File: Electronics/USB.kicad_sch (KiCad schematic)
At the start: 13 parts, among them IC4 USB2512B-AEZG, J24 USB_A_Stacked

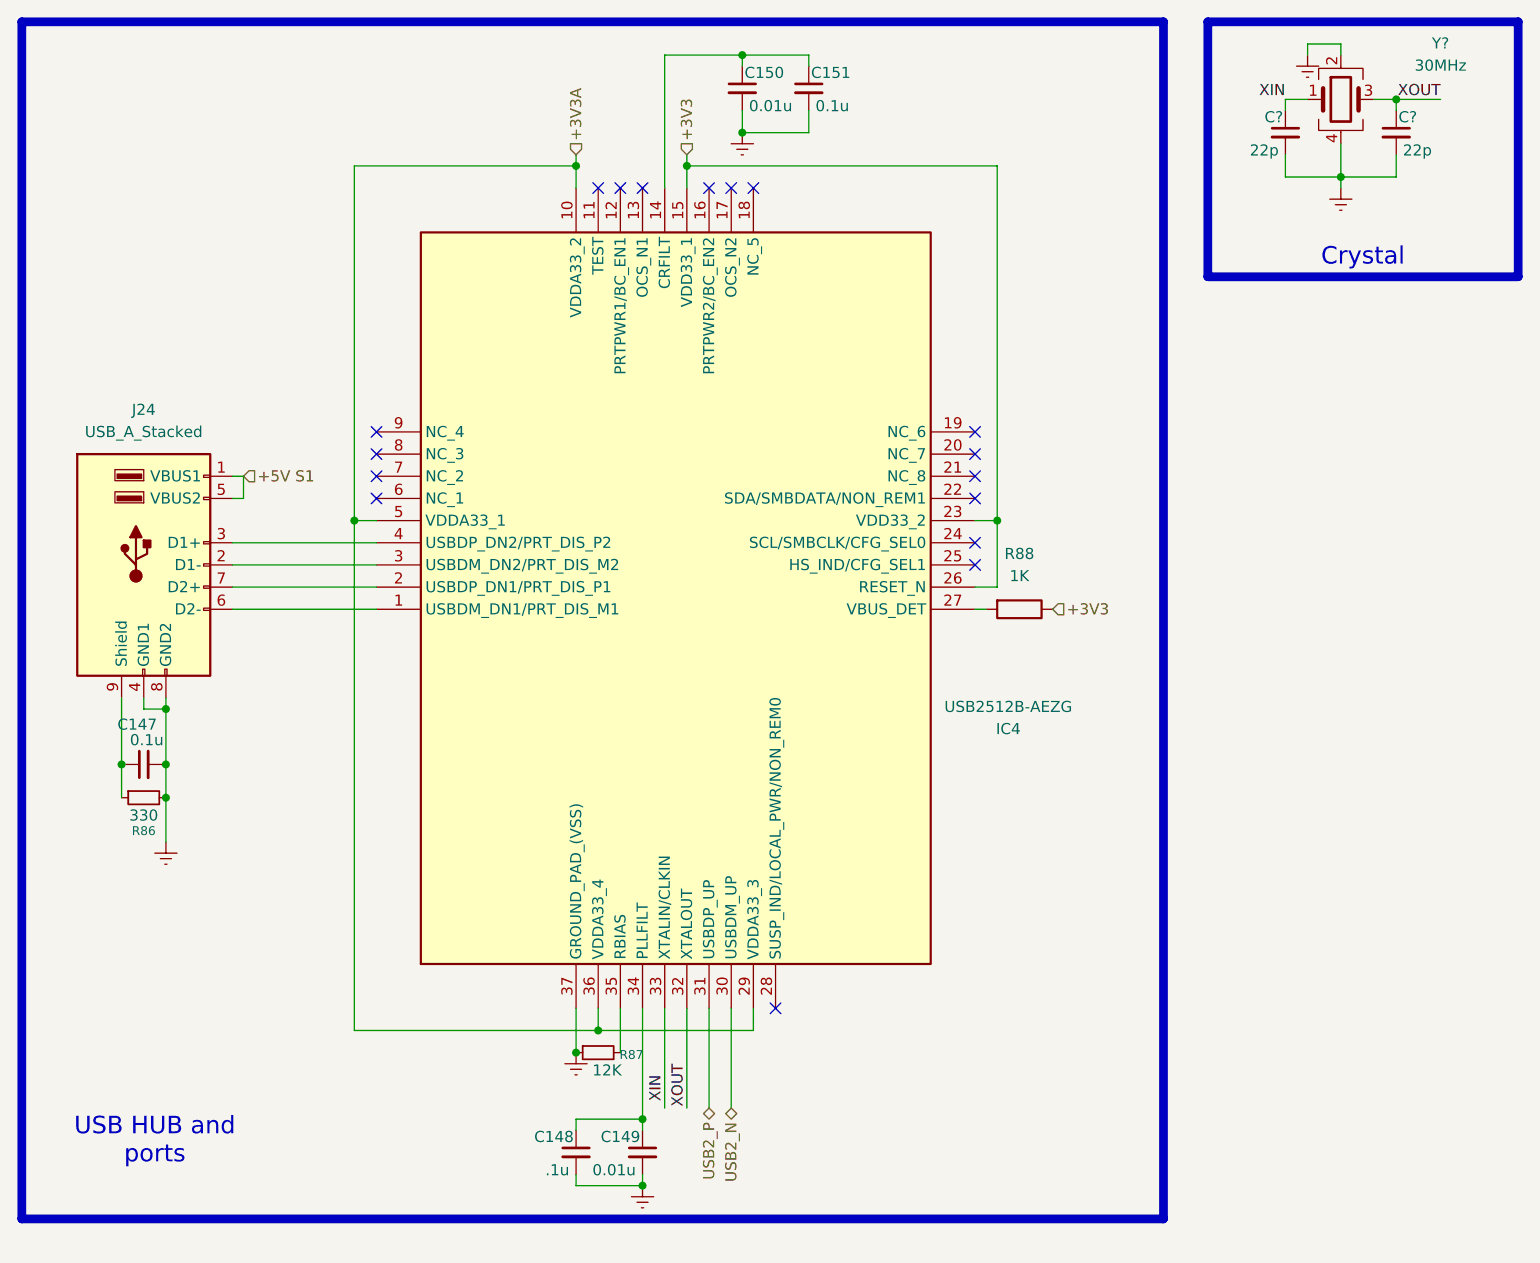
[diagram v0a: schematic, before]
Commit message: Power symbols changed and sata hub fixed schem
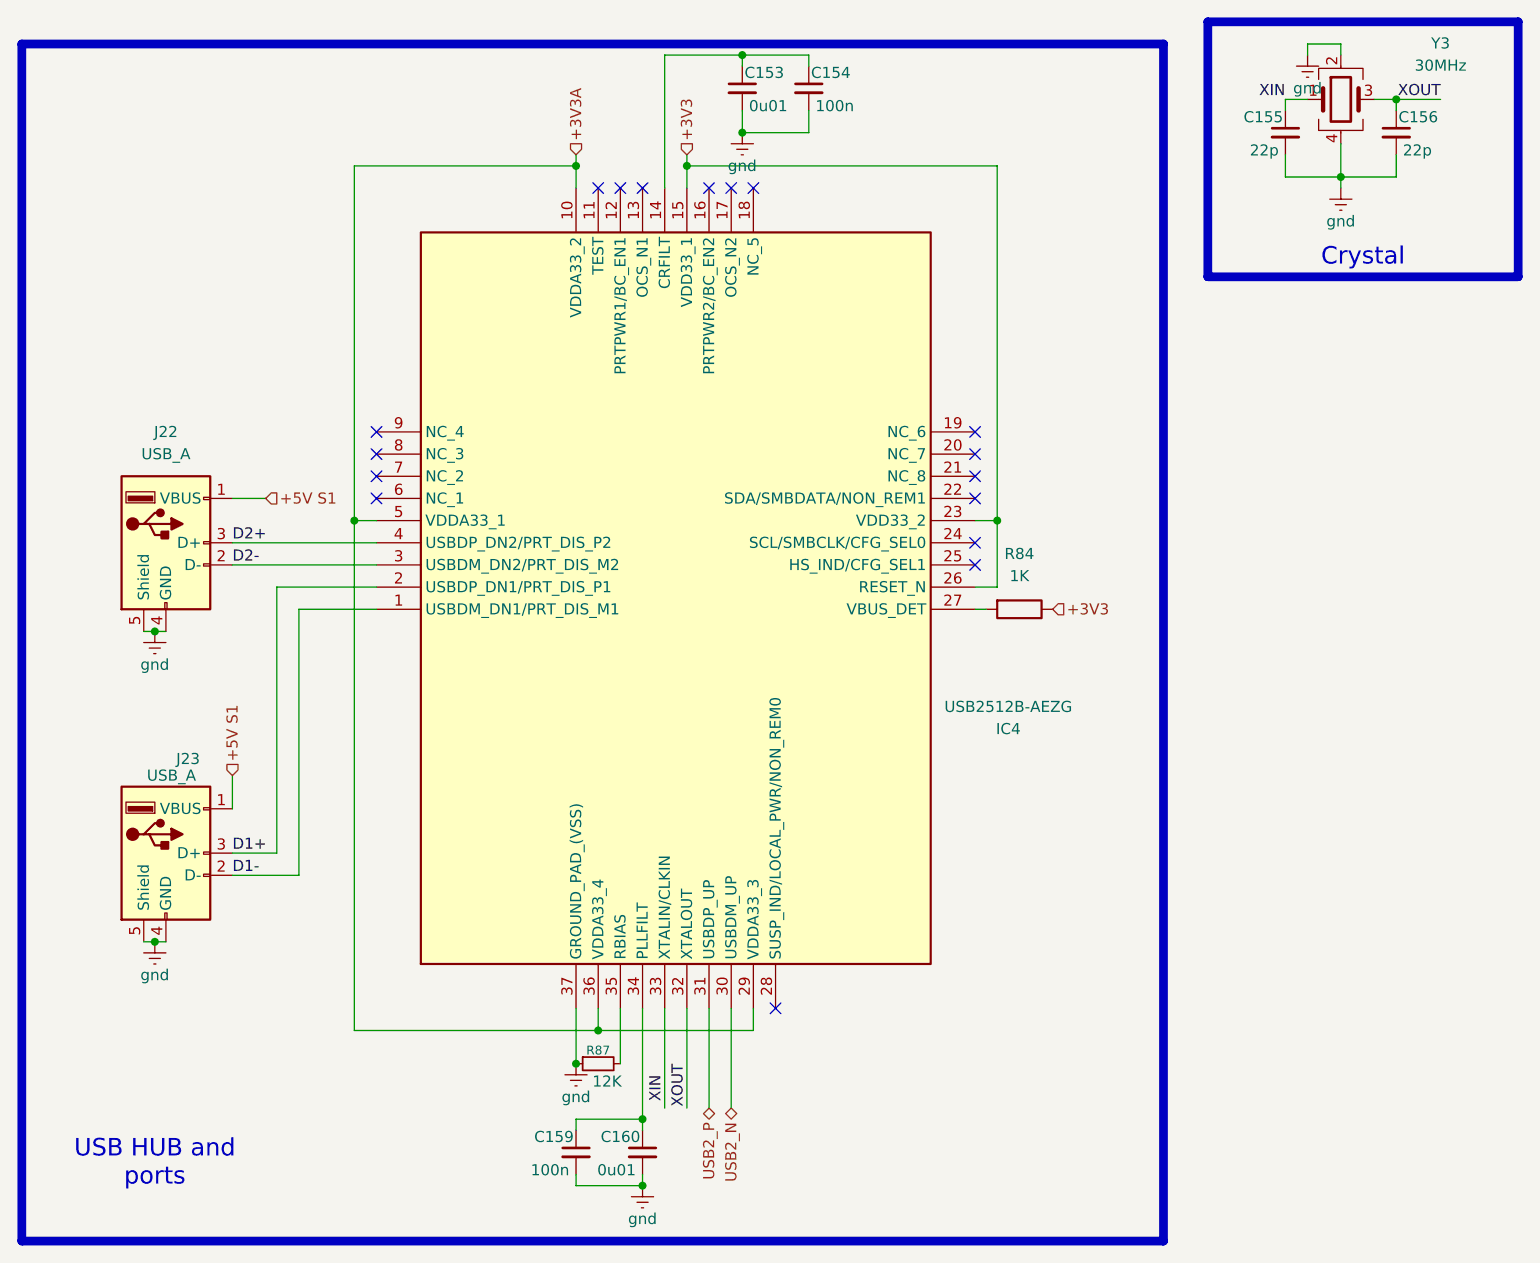
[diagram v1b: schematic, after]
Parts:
- removed C147: 0.1u, Capacitor_SMD:C_0603_1608Metric, symbol Device:C_Small
- removed J24: USB_A_Stacked, Connector_USB:USB_A_Wuerth_61400826021_Horizontal_Stacked, symbol Connector:USB_A_Stacked
- removed R86: 330, Resistor_SMD:R_0603_1608Metric, symbol Device:R_Small
- added J22, J23: USB_A, 482040001:CONN_48204-0001_MOL, symbol Connector:USB_A
- C153: renamed from C150; value 0.01u -> 0u01; footprint Capacitor_SMD:C_0603_1608Metric -> Capacitor_SMD:C_0402_1005Metric
- C154: renamed from C151; value 0.1u -> 100n
- C155, C156: renamed from C?; footprint Capacitor_SMD:C_0603_1608Metric -> Capacitor_SMD:C_0402_1005Metric
- C159: renamed from C148; value .1u -> 100n
- C160: renamed from C149; value 0.01u -> 0u01; footprint Capacitor_SMD:C_0603_1608Metric -> Capacitor_SMD:C_0402_1005Metric
- Y3: renamed from Y?; footprint (none) -> ABM8-30.000MHZ-B2-T:ABM810000MHZ12D2W
- renumbered R88 to R84
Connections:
- net +5V S1: now also J22.1 (VBUS), J23.1 (VBUS)
- net D1-: now reaches IC4.1 (USBDM_DN1/PRT_DIS_M1)
- net D1-: now also J23.2 (D-)
- net D1+: now reaches IC4.2 (USBDP_DN1/PRT_DIS_P1)
- net D1+: now also J23.3 (D+)
- net D2-: now reaches IC4.3 (USBDM_DN2/PRT_DIS_M2)
- net D2-: now also J22.2 (D-)
- net gnd: now reaches IC4.37 (GROUND_PAD_(VSS)), R87.1
- net gnd: now also C153.2, C154.2, C155.2, C156.2, C159.2, C160.2, Y3.2, Y3.4, J22.4 (GND), J22.5 (Shield), J23.4 (GND), J23.5 (Shield)
- net D2+: now reaches IC4.4 (USBDP_DN2/PRT_DIS_P2)
- net D2+: now also J22.3 (D+)
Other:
- moved on the sheet: R87
